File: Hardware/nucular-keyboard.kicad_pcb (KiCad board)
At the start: 2 copper layers, 48 x 26 mm, 34 parts, among them IC1 STM32L052R6Tx, J1 JAE_AA01B-S040VA1, J2 JAE_KX14-40K2D, J3 CONN_01X16, J4 CONN_01X03, Q1 IRLML6402, U1 MCP1700T-3302E/MB

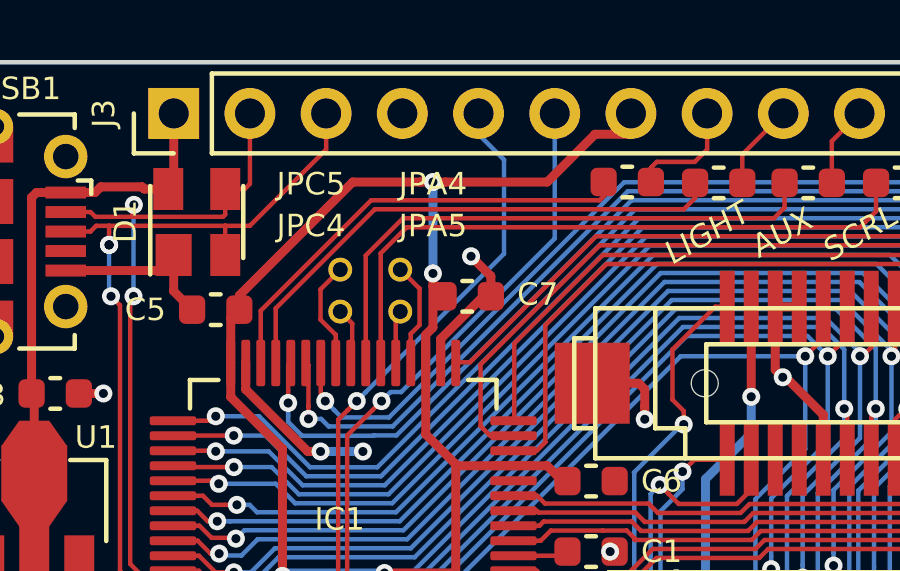
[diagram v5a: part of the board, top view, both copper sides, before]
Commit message: Add silkscreen to back side
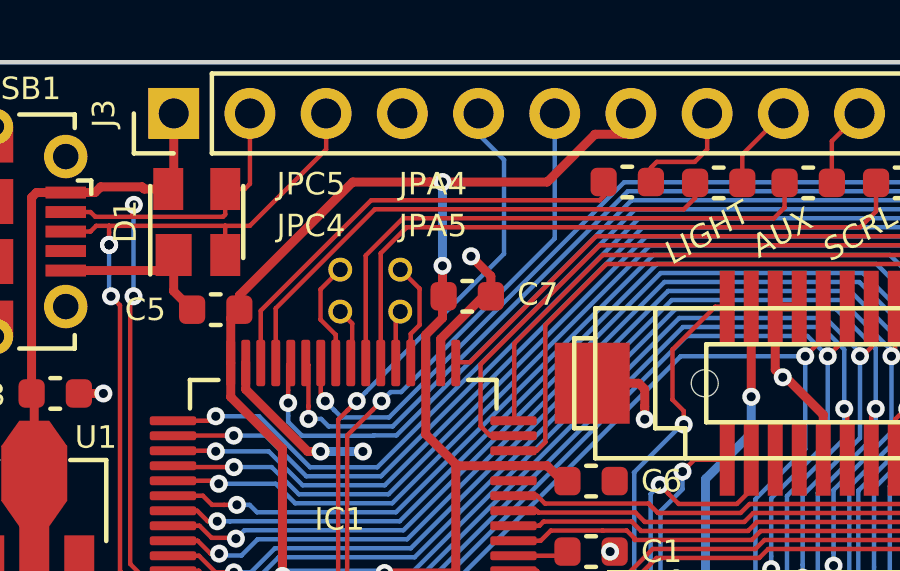
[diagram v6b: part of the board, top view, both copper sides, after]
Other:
- board text added: "GND"
- board text added: "RXD"
- board text added: "SWCLK"
- board text added: "SWDIO"
- board text added: "TXT"
- board text added: "USB D+"
- board text added: "USB D-"
- board text added: "VBUS"
- board text added: "VCC"
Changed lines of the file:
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@@
   (general
     (thickness 0.8)
-    (drawings 14)
+    (drawings 33)
     (tracks 1192)
     (zones 0)
@@
   (page A4)
   (layers
-    (0 F.Cu signal)
-    (31 B.Cu signal hide)
+    (0 F.Cu signal hide)
+    (31 B.Cu signal)
     (32 B.Adhes user hide)
     (33 F.Adhes user hide)
     (34 B.Paste user hide)
     (35 F.Paste user hide)
-    (36 B.SilkS user hide)
-    (37 F.SilkS user)
+    (36 B.SilkS user)
+    (37 F.SilkS user hide)
     (38 B.Mask user hide)
     (39 F.Mask user hide)
@@
     (42 Eco1.User user hide)
     (43 Eco2.User user hide)
-    (44 Edge.Cuts user hide)
+    (44 Edge.Cuts user)
     (45 Margin user hide)
     (46 B.CrtYd user hide)
@@
     )
   )
+  (gr_text SWCLK (at 65.278 83.312) (layer B.SilkS)
+    (effects (font (size 0.75 1) (thickness 0.15)) (justify mirror))
+  )
+  (gr_text SWDIO (at 65.024 78.232) (layer B.SilkS)
+    (effects (font (size 0.75 1) (thickness 0.15)) (justify mirror))
+  )
+  (gr_text GND (at 64.262 80.772) (layer B.SilkS)
+    (effects (font (size 0.75 1) (thickness 0.15)) (justify mirror))
+  )
+  (gr_text VBUS (at 67.818 64.262 90) (layer B.SilkS)
+    (effects (font (size 0.75 1) (thickness 0.15) italic) (justify mirror))
+  )
+  (gr_text "USB D+" (at 72.898 65.278 90) (layer B.SilkS)
+    (effects (font (size 0.75 1) (thickness 0.15) italic) (justify mirror))
+  )
+  (gr_text "USB D-" (at 70.358 65.278 90) (layer B.SilkS)
+    (effects (font (size 0.75 1) (thickness 0.15) italic) (justify mirror))
+  )
+  (gr_text GND (at 75.565 63.754 90) (layer B.SilkS)
+    (effects (font (size 0.75 1) (thickness 0.15) italic) (justify mirror))
+  )
+  (gr_text TXT (at 77.978 63.5 90) (layer B.SilkS)
+    (effects (font (size 0.75 1) (thickness 0.15) italic) (justify mirror))
+  )
+  (gr_text RXD (at 80.518 63.754 90) (layer B.SilkS)
+    (effects (font (size 0.75 1) (thickness 0.15) italic) (justify mirror))
+  )
+  (gr_text VCC (at 83.185 63.754 90) (layer B.SilkS)
+    (effects (font (size 0.75 1) (thickness 0.15) italic) (justify mirror))
+  )
+  (gr_text MIC (at 103.124 63.246 90) (layer B.SilkS)
+    (effects (font (size 0.75 0.75) (thickness 0.15) italic) (justify mirror))
+  )
+  (gr_text LIGHT (at 85.5 64.008 90) (layer B.SilkS)
+    (effects (font (size 0.75 0.75) (thickness 0.15) italic) (justify mirror))
+  )
+  (gr_text AUX (at 88 63.57 90) (layer B.SilkS)
+    (effects (font (size 0.75 0.75) (thickness 0.15) italic) (justify mirror))
+  )
+  (gr_text SCRL (at 90.6 63.754 90) (layer B.SilkS)
+    (effects (font (size 0.75 0.75) (thickness 0.15) italic) (justify mirror))
+  )
+  (gr_text NUM (at 93.2 63.57 90) (layer B.SilkS)
+    (effects (font (size 0.75 0.75) (thickness 0.15) italic) (justify mirror))
+  )
+  (gr_text CAPS (at 95.7 63.754 90) (layer B.SilkS)
+    (effects (font (size 0.75 0.75) (thickness 0.15) italic) (justify mirror))
+  )
+  (gr_text PWR (at 98.2 63.57 90) (layer B.SilkS)
+    (effects (font (size 0.75 0.75) (thickness 0.15) italic) (justify mirror))
+  )
+  (gr_text MUTE (at 100.584 63.754 90) (layer B.SilkS)
+    (effects (font (size 0.75 0.75) (thickness 0.15) italic) (justify mirror))
+  )
+  (gr_text GND (at 105.918 63.754 90) (layer B.SilkS)
+    (effects (font (size 0.75 1) (thickness 0.15) italic) (justify mirror))
+  )
   (gr_line (start 60 59) (end 108 59) (layer Edge.Cuts) (width 0.15))
   (gr_line (start 60 85) (end 60 59) (layer Edge.Cuts) (width 0.15))
@@
   (segment (start 69.65 70.15941) (end 71.372464 71.881874) (width 0.3) (layer F.Cu) (net 1))
   (segment (start 65.375 78.45) (end 69.46935 78.45) (width 0.3) (layer F.Cu) (net 1))
-  (via (at 76.3905 66.040002) (size 0.6) (drill 0.3) (layers F.Cu B.Cu) (net 1))
-  (segment (start 76.3905 67.842743) (end 76.3905 66.464266) (width 0.3) (layer F.Cu) (net 1))
-  (segment (start 76.15 68.083243) (end 76.3905 67.842743) (width 0.3) (layer F.Cu) (net 1))
   (segment (start 77.15 72.4) (end 76.15 71.4) (width 0.3) (layer F.Cu) (net 1))
-  (segment (start 76.3905 66.464266) (end 76.3905 66.040002) (width 0.3) (layer F.Cu) (net 1))
   (segment (start 76.15 71.4) (end 76.15 68.083243) (width 0.3) (layer F.Cu) (net 1))
-  (segment (start 76.3905 66.040002) (end 76.3905 62.992) (width 0.3) (layer B.Cu) (net 1))
-  (segment (start 75.966236 62.992) (end 76.3905 62.992) (width 0.3) (layer F.Cu) (net 1))
+  (segment (start 76.708 66.210264) (end 76.708 65.786) (width 0.3) (layer F.Cu) (net 1))
+  (via (at 76.708 65.786) (size 0.6) (drill 0.3) (layers F.Cu B.Cu) (net 1))
+  (segment (start 76.708 67.525243) (end 76.708 66.210264) (width 0.3) (layer F.Cu) (net 1))
+  (segment (start 76.15 68.083243) (end 76.708 67.525243) (width 0.3) (layer F.Cu) (net 1))
+  (via (at 76.708 62.992) (size 0.6) (drill 0.3) (layers F.Cu B.Cu) (net 1))
+  (segment (start 76.283736 62.992) (end 76.708 62.992) (width 0.3) (layer F.Cu) (net 1))
+  (segment (start 76.708 65.786) (end 76.708 62.992) (width 0.3) (layer B.Cu) (net 1))
+  (segment (start 69.9375 67.2465) (end 69.9375 66.7715) (width 0.3) (layer F.Cu) (net 1))
+  (segment (start 80.2005 62.992) (end 77.132264 62.992) (width 0.3) (layer F.Cu) (net 1))
+  (segment (start 81.7925 61.4) (end 80.2005 62.992) (width 0.3) (layer F.Cu) (net 1))
+  (segment (start 77.132264 62.992) (end 76.708 62.992) (width 0.3) (layer F.Cu) (net 1))
   (segment (start 82.99 61.4) (end 81.7925 61.4) (width 0.3) (layer F.Cu) (net 1))
-  (via (at 76.3905 62.992) (size 0.6) (drill 0.3) (layers F.Cu B.Cu) (net 1))
-  (segment (start 73.717 62.992) (end 75.966236 62.992) (width 0.3) (layer F.Cu) (net 1))
-  (segment (start 81.7925 61.4) (end 80.2005 62.992) (width 0.3) (layer F.Cu) (net 1))
+  (segment (start 73.717 62.992) (end 76.283736 62.992) (width 0.3) (layer F.Cu) (net 1))
   (segment (start 69.9375 66.7715) (end 73.717 62.992) (width 0.3) (layer F.Cu) (net 1))
-  (segment (start 69.9375 67.2465) (end 69.9375 66.7715) (width 0.3) (layer F.Cu) (net 1))
-  (segment (start 80.2005 62.992) (end 76.814764 62.992) (width 0.3) (layer F.Cu) (net 1))
-  (segment (start 76.814764 62.992) (end 76.3905 62.992) (width 0.3) (layer F.Cu) (net 1))
   (segment (start 87.5 77.2) (end 87.5 78.1) (width 0.3) (layer F.Cu) (net 2) (status 10))
   (via (at 87.55 78.15) (size 0.6) (drill 0.3) (layers F.Cu B.Cu) (net 2))
